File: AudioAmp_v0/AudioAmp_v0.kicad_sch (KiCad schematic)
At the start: 50 parts, among them J1 AudioJack3, J2 Conn_01x02_Pin, J3 Connector_RCJ-042, J4 Connector_RCJ-042, J5 AudioJack3, J6 Conn_01x02_Pin, J7 Conn_01x02_Pin, Q1 NMOS_ MTB7D0N6RJ3, Q2 PMOS_MTP4835I3, Q3 NMOS_BSS138, Q4 PMOS_BSS84, SW1 SW_DPDT_x2, SW2 SW_DPDT_x2, U1 MAU108, U2 NJM5532, U3 NJM5532

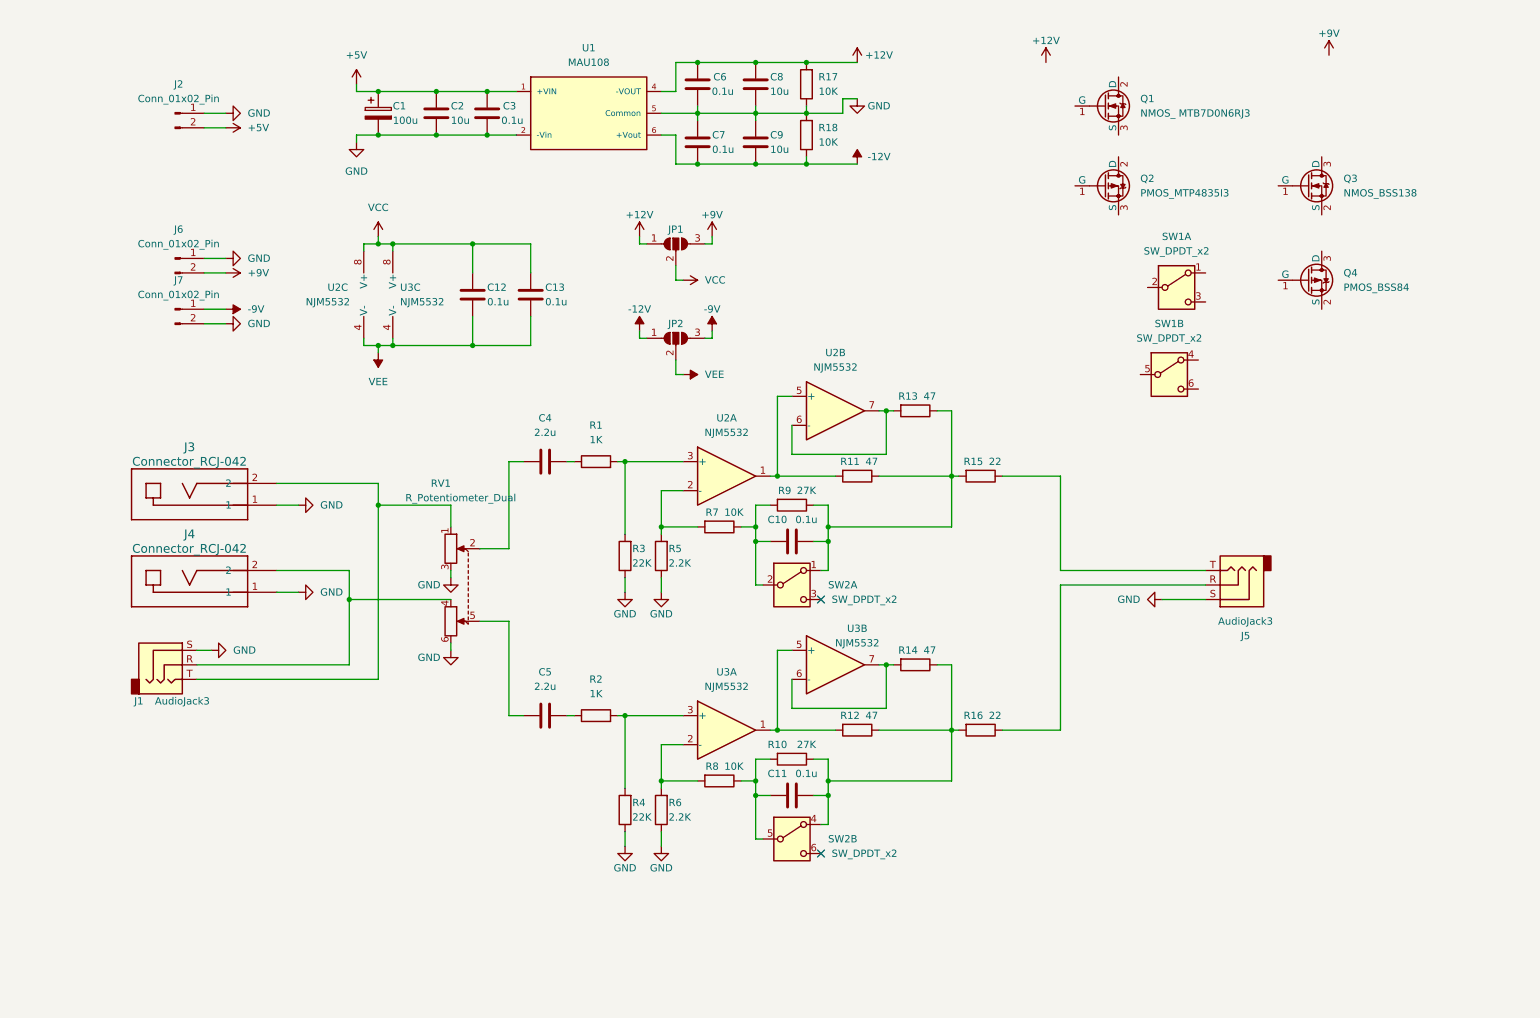
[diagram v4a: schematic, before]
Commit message: 電源切り替え回路完成
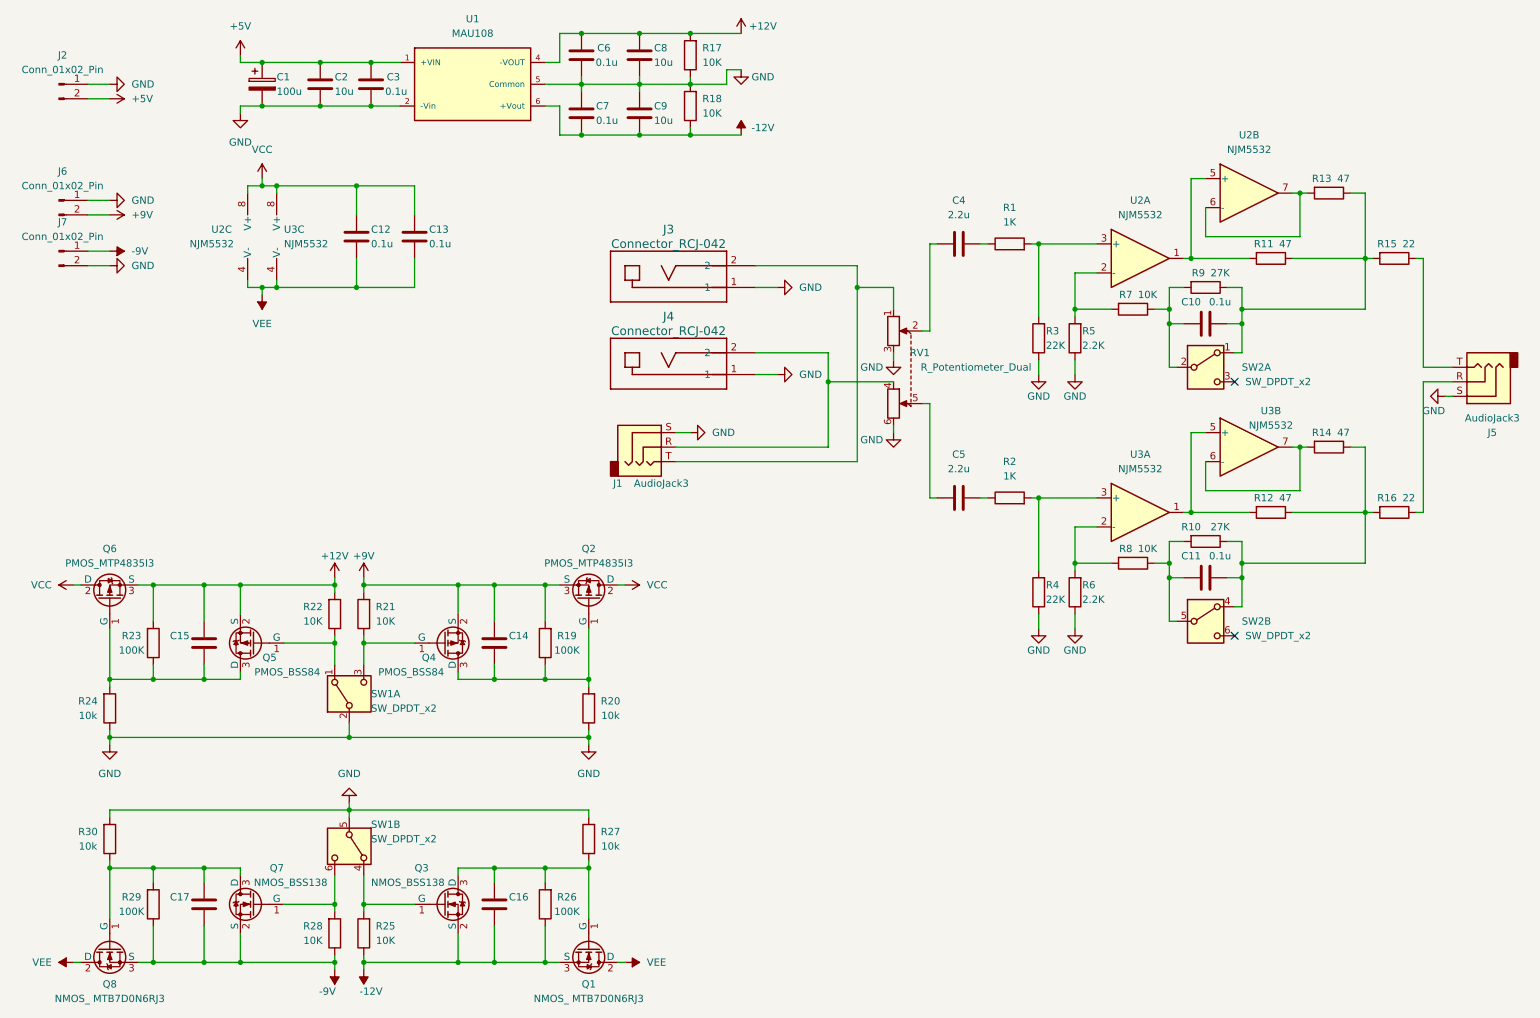
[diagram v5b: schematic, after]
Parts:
- removed JP1, JP2: SolderJumper_3_Open, Jumper:SolderJumper-3_P2.0mm_Open_TrianglePad1.0x1.5mm, symbol Jumper:SolderJumper_3_Open
- added C14, C15, C16, C17: ~, Capacitor_SMD:C_0805_2012Metric, symbol Device:C
- added Q5: PMOS_BSS84, Package_TO_SOT_SMD:TSOT-23, symbol Device:Q_PMOS_GSD
- added Q6: PMOS_MTP4835I3, Package_TO_SOT_SMD:TO-252-2, symbol Device:Q_PMOS_GDS
- added Q7: NMOS_BSS138, Package_TO_SOT_SMD:SOT-23, symbol Device:Q_NMOS_GSD
- added Q8: NMOS_ MTB7D0N6RJ3, Package_TO_SOT_SMD:TO-252-2, symbol Device:Q_NMOS_GDS
- added R19, R23, R26, R29: 100K, Resistor_SMD:R_0603_1608Metric, symbol Device:R
- added R20, R24, R27, R30: 10k, Resistor_SMD:R_0603_1608Metric, symbol Device:R
- added R21, R22, R25, R28: 10K, Resistor_SMD:R_0603_1608Metric, symbol Device:R
- R17, R18: footprint Resistor_THT:R_Axial_DIN0207_L6.3mm_D2.5mm_P10.16mm_Horizontal -> Resistor_SMD:R_0603_1608Metric
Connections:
- net +12V: now also C15.1, Q5.2 (S), Q6.3 (S), R22.2, R23.2
- net +9V: now also Q2.3 (S), Q4.2 (S), C14.1, R19.2, R21.2
- net -12V: now also Q1.3 (S), Q3.2 (S), C16.2, R25.1, R26.1
- net -9V: now also C17.2, Q7.2 (S), Q8.3 (S), R28.1, R29.1
- net GND: now also SW1.2 (B), SW1.5 (B), R20.1, R24.1, R27.2, R30.2
- net VCC: now also Q2.2 (D), Q6.2 (D)
- net VEE: now also Q1.2 (D), Q8.2 (D)
- net at SW1.4 (A): now also Q3.1 (G), R25.2
- net at SW1.6 (C): now also Q7.1 (G), R28.2
- net at SW1.1 (A): now also Q5.1 (G), R22.1
- net at SW1.3 (C): now also Q4.1 (G), R21.1
- net at Q3.3 (D): now also Q1.1 (G), C16.1, R26.2, R27.1
- net at Q2.1 (G): now also Q4.3 (D), C14.2, R19.1, R20.2
- new net: C17.1, Q7.3 (D), Q8.1 (G), R29.2, R30.1
- new net: C15.2, Q5.3 (D), Q6.1 (G), R23.1, R24.2
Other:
- moved on the sheet: C1, C10, C11, C12, C13, C2, C3, C4, C5, C6, C7, C8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

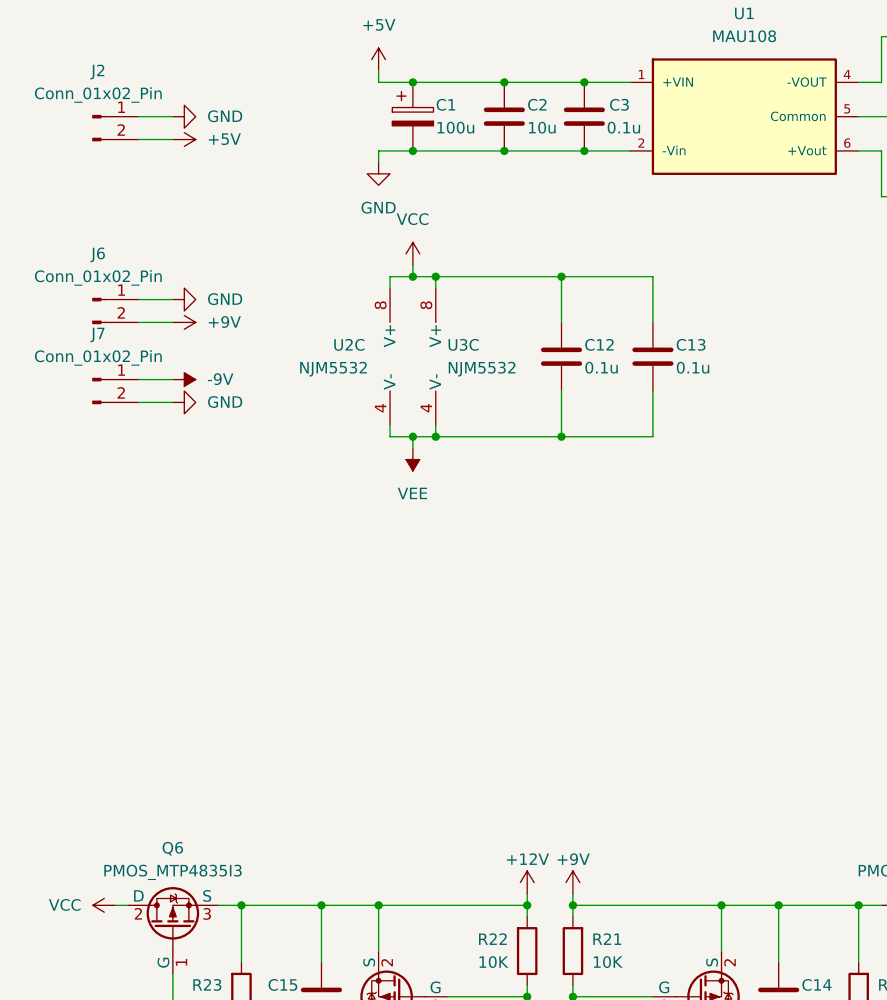
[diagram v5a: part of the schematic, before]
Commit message: 基板サイズ確定（秋月B基板互換）
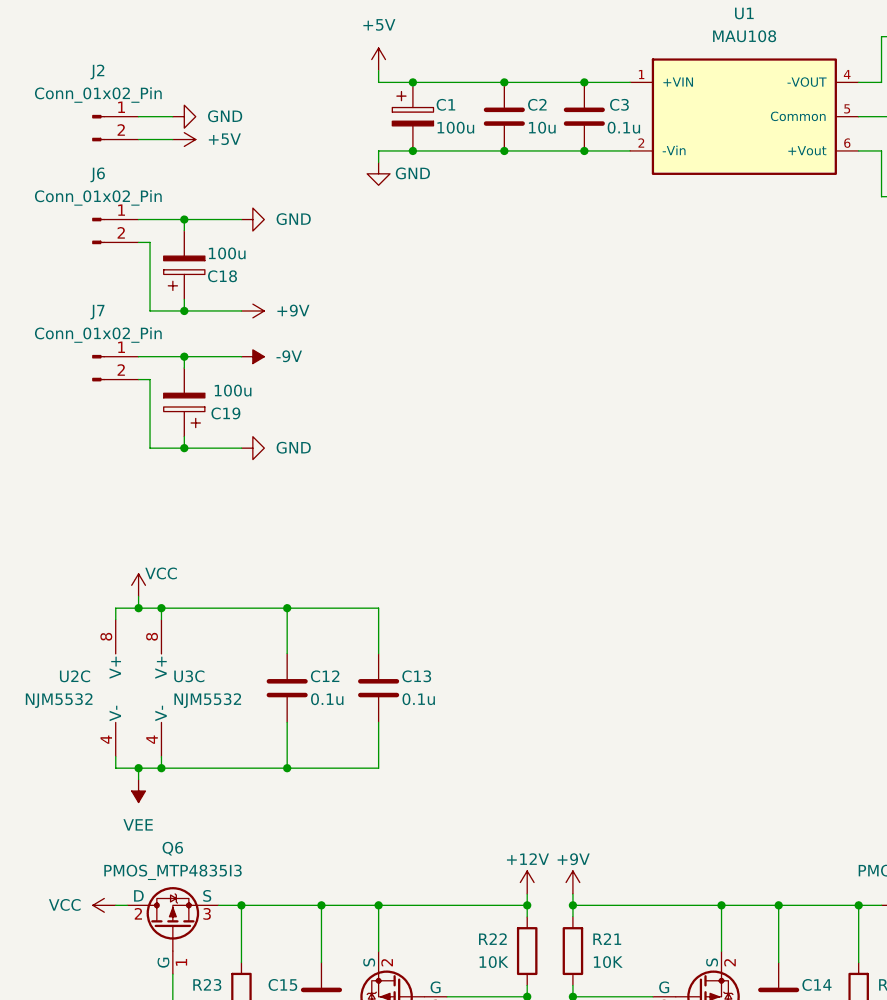
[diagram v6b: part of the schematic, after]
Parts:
- added C18, C19: 100u, Capacitor_SMD:CP_Elec_6.3x5.7, symbol Device:C_Polarized
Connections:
- net +9V: now also C18.1
- net -9V: now also C19.2
- net GND: now also C18.2, C19.1
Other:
- moved on the sheet: C12, C13, J6, J7, U2C, U3C

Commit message: 最低限完成
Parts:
- added D1, D2, D3, D4: LED, symbol Device:LED
- added R31, R32, R33, R34: 10K, Resistor_THT:R_Axial_DIN0207_L6.3mm_D2.5mm_P10.16mm_Horizontal, symbol Device:R
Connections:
- net +12V: now also D2.2 (A)
- net +5V: now also D1.2 (A)
- net +9V: now also D3.2 (A)
- net -12V: now also R32.1
- net -9V: now also R33.1
- net GND: now also R31.1
- net VCC: now also D4.2 (A)
- net VEE: now also R34.1
- new net: D2.1 (K), R32.2
- new net: D1.1 (K), R31.2
- new net: D3.1 (K), R33.2
- new net: D4.1 (K), R34.2

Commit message: LED追加
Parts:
- D1, D2, D3, D4: footprint (none) -> LED_THT:LED_D3.0mm
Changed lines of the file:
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@@
       (effects (font (size 1.27 1.27)))
     )
-    (property "Footprint" "" (at 72.39 53.34 0)
+    (property "Footprint" "LED_THT:LED_D3.0mm" (at 72.39 53.34 0)
       (effects (font (size 1.27 1.27)) hide)
     )
@@
       (effects (font (size 1.27 1.27)))
     )
-    (property "Footprint" "" (at 72.39 60.96 0)
+    (property "Footprint" "LED_THT:LED_D3.0mm" (at 72.39 60.96 0)
       (effects (font (size 1.27 1.27)) hide)
     )
@@
       (effects (font (size 1.27 1.27)))
     )
-    (property "Footprint" "" (at 72.39 68.58 0)
+    (property "Footprint" "LED_THT:LED_D3.0mm" (at 72.39 68.58 0)
       (effects (font (size 1.27 1.27)) hide)
     )
@@
       (effects (font (size 1.27 1.27)))
     )
-    (property "Footprint" "" (at 72.39 76.2 0)
-      (effects (font (size 1.27 1.27)) hide)
-    )
+    (property "Footprint" "LED_THT:LED_D3.0mm" (at 72.39 76.2 0)
+      (effects (font (size 1.27 1.27)) hide)
+    )
